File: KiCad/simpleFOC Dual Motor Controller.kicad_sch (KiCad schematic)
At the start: 17 parts, among them J101 Conn_01x04, J102 Conn_ARM_JTAG_SWD_10, SW101 TS-1088-AR02016, U101 STM32F103C8Tx, U102 XT60H-M

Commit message: updated configuration for new mosfets
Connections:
- net GAIN1: now reaches U101.2 (PC13)
- net GAIN2: now reaches U101.4 (PC15)
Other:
- sheet Motor Driver 1 ports: added Gain, ~{FAULT}; removed FAULT
- sheet Motor Driver 2 ports: added Gain, ~{FAULT}; removed FAULT
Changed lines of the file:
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@@
 	(wire
 		(pts
+			(xy 116.84 87.63) (xy 107.95 87.63)
+		)
+		(stroke
+			(width 0)
+			(type default)
+		)
+	)
+	(wire
+		(pts
 			(xy 135.89 149.86) (xy 134.62 149.86)
 		)
@@
 	(wire
 		(pts
+			(xy 116.84 92.71) (xy 107.95 92.71)
+		)
+		(stroke
+			(width 0)
+			(type default)
+		)
+	)
+	(wire
+		(pts
 			(xy 69.85 123.19) (xy 78.74 123.19)
 		)
@@
 	(wire
 		(pts
+			(xy 255.27 105.41) (xy 264.16 105.41)
+		)
+		(stroke
+			(width 0)
+			(type default)
+		)
+	)
+	(wire
+		(pts
 			(xy 50.8 63.5) (xy 58.42 63.5)
 		)
@@
 	(wire
 		(pts
+			(xy 255.27 58.42) (xy 264.16 58.42)
+		)
+		(stroke
+			(width 0)
+			(type default)
+		)
+	)
+	(wire
+		(pts
 			(xy 116.84 118.11) (xy 107.95 118.11)
 		)
@@
 		)
 	)
+	(label "GAIN1"
+		(at 107.95 87.63 0)
+		(effects
+			(font
+				(size 1.27 1.27)
+			)
+			(justify left bottom)
+		)
+	)
 	(label "sns_cs1"
 		(at 161.29 97.79 180)
@@
 		)
 	)
+	(label "GAIN2"
+		(at 107.95 92.71 0)
+		(effects
+			(font
+				(size 1.27 1.27)
+			)
+			(justify left bottom)
+		)
+	)
 	(label "FAULT1"
 		(at 107.95 128.27 0)
@@
 		)
 	)
+	(label "GAIN1"
+		(at 264.16 58.42 180)
+		(effects
+			(font
+				(size 1.27 1.27)
+			)
+			(justify right bottom)
+		)
+	)
 	(label "ctrl_scl"
 		(at 39.37 71.12 180)
@@
 		)
 	)
+	(label "GAIN2"
+		(at 264.16 105.41 180)
+		(effects
+			(font
+				(size 1.27 1.27)
+			)
+			(justify right bottom)
+		)
+	)
 	(label "CHCn2"
 		(at 205.74 127 0)
@@
 			)
 		)
-		(pin "FAULT" output
-			(at 214.63 60.96 180)
-			(effects
-				(font
-					(size 1.27 1.27)
-				)
-				(justify left)
-			)
-		)
 		(pin "INHA" input
 			(at 214.63 66.04 180)
@@
 			)
 		)
+		(pin "Gain" input
+			(at 255.27 58.42 0)
+			(effects
+				(font
+					(size 1.27 1.27)
+				)
+				(justify right)
+			)
+		)
+		(pin "~{FAULT}" output
+			(at 214.63 60.96 180)
+			(effects
+				(font
+					(size 1.27 1.27)
+				)
+				(justify left)
+			)
+		)
 		(instances
 			(project "simpleFOC Dual Motor Controller"
@@
 			)
 		)
-		(pin "FAULT" output
-			(at 214.63 107.95 180)
-			(effects
-				(font
-					(size 1.27 1.27)
-				)
-				(justify left)
-			)
-		)
 		(pin "INHA" input
 			(at 214.63 113.03 180)
@@
 			(effects
 				(font
+					(size 1.27 1.27)
+				)
+				(justify left)
+			)
+		)
+		(pin "Gain" input
+			(at 255.27 105.41 0)
+			(effects
+				(font
+					(size 1.27 1.27)
+				)
+				(justify right)
+			)
+		)
+		(pin "~{FAULT}" output
+			(at 214.63 107.95 180)
+			(effects
+				(font

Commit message: started laying out
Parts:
- removed C106, C107: 100n, symbol Device:C_Small
- removed D103: DSK26_C7502712, easyeda2kicad:SOD-123FL_L2.7-W1.8-LS3.8-RD, symbol easyeda2kicad:DSK26_C7502712
- removed H101, H102: MountingHole, MountingHole:MountingHole_4.3mm_M4, symbol Mechanical:MountingHole
- removed J102: Conn_ARM_JTAG_SWD_10, symbol Connector:Conn_ARM_JTAG_SWD_10
- removed U101: STM32F103C8Tx, Package_QFP:LQFP-48_7x7mm_P0.5mm, symbol MCU_ST_STM32F1:STM32F103C8Tx
- added C111: C_Small, Capacitor_SMD:C_01005_0402Metric, symbol Device:C_Small
- added D102, D107: B16WS_C7420327, easyeda2kicad:SOD-323_L1.7-W1.3-LS2.5-FD, symbol easyeda2kicad:B16WS_C7420327
- added D105, D106: H5VL06B, easyeda2kicad:X3-DFN0603-2_L0.6-W0.3-BI, symbol easyeda2kicad:H5VL06B
- added J102: USB_C_Receptacle_USB2.0_14P, Connector_USB:USB_C_Receptacle_HCTL_HC-TYPE-C-16P-01A, symbol Connector:USB_C_Receptacle_USB2.0_14P
- added R107, R108: 5.1k, PCM_SparkFun-Resistor:R_0402_1005Metric, symbol Device:R_Small
- added R109: 10k, PCM_SparkFun-Resistor:R_0402_1005Metric, symbol Device:R_Small
- added U101: XC6206P332MR, easyeda2kicad:SOT-23-3_L2.9-W1.6-P1.90-LS2.8-BR, symbol easyeda2kicad:XC6206P332MR
- added U103: ESP32-S3-WROOM-1, RF_Module:ESP32-S3-WROOM-1, symbol RF_Module:ESP32-S3-WROOM-1
- C103: footprint (none) -> Capacitor_SMD:C_01005_0402Metric
- C104: value 100n -> 22u; footprint (none) -> Capacitor_SMD:C_1206_3216Metric
- C105: value 100n -> 1u; footprint (none) -> Capacitor_SMD:C_01005_0402Metric
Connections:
- net +3.3V: now also R109.1, U101.2 (Vout), U103.2 (3V3); no longer C102.1, C105.1
- net CAL1: now also U103.31 (IO38)
- net CAL2: now also U103.8 (IO15)
- net CHA1: now also U103.35 (IO42)
- net CHA2: now also U103.5 (IO5)
- net CHB1: now also U103.34 (IO41)
- net CHB2: now also U103.6 (IO6)
- net CHC1: now also U103.33 (IO40)
- net CHC2: now also U103.7 (IO7)
- net EN1: now also U103.32 (IO39)
- net EN2: now also U103.12 (IO8)
- net FAULT1: now also U103.28 (IO35)
- net FAULT2: now also U103.18 (IO10)
- net GAIN1: now also U103.29 (IO36)
- net GAIN2: now also U103.19 (IO11)
- net GND: now also C111.2, D105.1 (C), D106.1 (C), J102.A1 (GND), J102.A12 (GND), J102.B1 (GND), J102.B12 (GND), J102.SH (SHIELD), R107.2, R108.2, U101.1 (GND), U103.1 (GND), U103.40 (GND), U103.41 (GND)
- net ctrl_scl: now also U103.20 (IO12)
- net ctrl_sda: now also U103.21 (IO13)
- net snsA1: now also U103.39 (IO1)
- net snsA2: now also U103.9 (IO16)
- net snsB1: now also U103.38 (IO2)
- net snsB2: now also U103.10 (IO17)
- net snsC1: now also U103.4 (IO4)
- net snsC2: now also U103.11 (IO18)
- net sns_cs1: now also U103.17 (IO9)
- net sns_cs2: now also U103.23 (IO21)
- net sns_miso: now also U103.24 (IO47)
- net sns_mosi: now also U103.25 (IO48)
- net sns_sck: now also U103.22 (IO14)
- net ~{rst}: now also C111.1, R109.2, U103.3 (EN)
- net at D104.1 (K), J101.4 (Pin_4): now also D107.1 (A)
- new net: J102.B5 (CC2), R108.1
- new net: D102.1 (A), J102.A4 (VBUS), J102.A9 (VBUS), J102.B4 (VBUS), J102.B9 (VBUS)
- new net: J102.A5 (CC1), R107.1
- new net +5V: C102.1, C105.1, D102.2 (K), D107.2 (K), U101.3 (Vin)
- new net D+: D106.2 (A), J102.A6 (D+), J102.B6 (D+), U103.14 (USB_D+)
- new net D-: D105.2 (A), J102.A7 (D-), J102.B7 (D-), U103.13 (USB_D-)
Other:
- sheet Motor Driver 1 ports: added ~{HI-Z}; removed INLA, INLB, INLC
- sheet Motor Driver 2 ports: added ~{HI-Z}; removed INLA, INLB, INLC
- moved on the sheet: C103, SW101

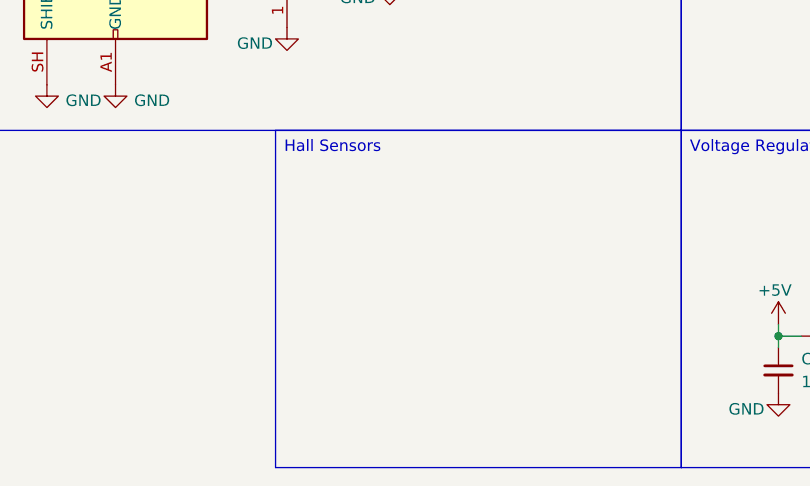
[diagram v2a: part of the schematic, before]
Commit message: added hall connectors
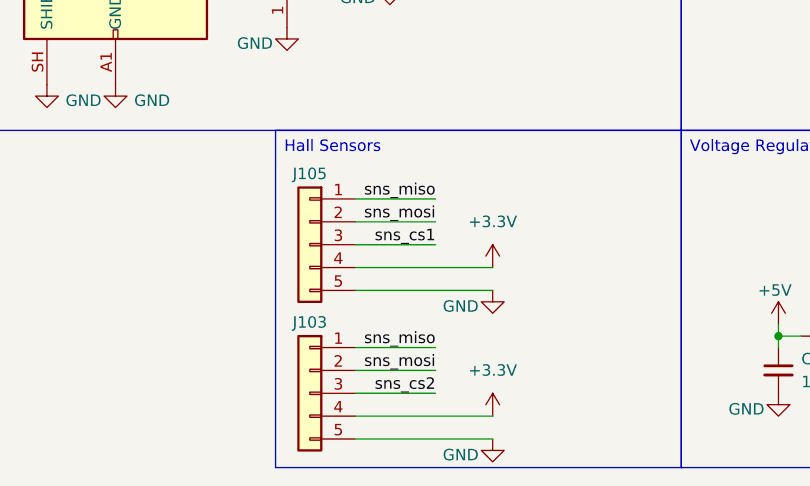
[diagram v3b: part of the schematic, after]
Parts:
- added J103, J105: Conn_01x05_2.0mm, Connector_JST:JST_PH_B5B-PH-K_1x05_P2.00mm_Vertical, symbol PCM_SparkFun-Connector:Conn_01x05_P2.0mm_Socket_Vertical_PTH
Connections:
- net +3.3V: now also J103.4 (Pin_4), J105.4 (Pin_4)
- net GND: now also J103.5 (Pin_5), J105.5 (Pin_5)
- net sns_cs1: now also J105.3 (Pin_3)
- net sns_cs2: now also J103.3 (Pin_3)
- net sns_miso: now also J103.1 (Pin_1), J105.1 (Pin_1)
- net sns_mosi: now also J103.2 (Pin_2), J105.2 (Pin_2)

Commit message: started routing
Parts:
- C105: footprint Capacitor_SMD:C_01005_0402Metric -> Capacitor_SMD:C_0402_1005Metric
- J101: footprint PCM_SparkFun-Connector:JST_1x04_P2.0mm_Vertical_PTH -> Connector_JST:JST_PH_B4B-PH-K_1x04_P2.00mm_Vertical
- R108: footprint PCM_SparkFun-Resistor:R_0402_1005Metric -> Resistor_SMD:R_0402_1005Metric
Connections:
- net CAL1: now also U103.12 (IO8); no longer U103.31 (IO38)
- net CAL2: now also U103.31 (IO38); no longer U103.8 (IO15)
- net CHA2: now also U103.30 (IO37); no longer U103.5 (IO5)
- net CHB1: now also U103.18 (IO10); no longer U103.34 (IO41)
- net CHB2: now also U103.29 (IO36); no longer U103.6 (IO6)
- net CHC1: now also U103.6 (IO6); no longer U103.33 (IO40)
- net CHC2: now also U103.28 (IO35); no longer U103.7 (IO7)
- net EN1: now also U103.8 (IO15); no longer U103.32 (IO39)
- net EN2: now also U103.32 (IO39); no longer U103.12 (IO8)
- net FAULT1: now also U103.7 (IO7); no longer U103.28 (IO35)
- net FAULT2: now also U103.34 (IO41); no longer U103.18 (IO10)
- net GAIN1: now also U103.19 (IO11); no longer U103.29 (IO36)
- net GAIN2: now also U103.33 (IO40); no longer U103.19 (IO11)
- net snsA1: now also U103.11 (IO18); no longer U103.39 (IO1)
- net snsA2: now also U103.39 (IO1); no longer U103.9 (IO16)
- net snsB1: now also U103.10 (IO17); no longer U103.38 (IO2)
- net snsB2: now also U103.38 (IO2); no longer U103.10 (IO17)
- net snsC2: now also U103.22 (IO14); no longer U103.11 (IO18)
- net sns_sck: now also U103.15 (IO3); no longer U103.22 (IO14)
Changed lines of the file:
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@@
 	(wire
 		(pts
-			(xy 130.81 175.26) (xy 132.08 175.26)
+			(xy 130.81 175.26) (xy 133.35 175.26)
 		)
 		(stroke
@@
 	(wire
 		(pts
-			(xy 109.22 120.65) (xy 118.11 120.65)
-		)
-		(stroke
-			(width 0)
-			(type default)
-		)
-	)
-	(wire
-		(pts
 			(xy 266.7 102.87) (xy 266.7 55.88)
 		)
@@
 	(wire
 		(pts
+			(xy 109.22 87.63) (xy 118.11 87.63)
+		)
+		(stroke
+			(width 0)
+			(type default)
+		)
+	)
+	(wire
+		(pts
 			(xy 31.75 66.04) (xy 44.45 66.04)
 		)
@@
 	(wire
 		(pts
-			(xy 118.11 92.71) (xy 109.22 92.71)
-		)
-		(stroke
-			(width 0)
-			(type default)
-		)
-	)
-	(wire
-		(pts
 			(xy 86.36 49.53) (xy 86.36 48.26)
 		)
@@
 	(wire
 		(pts
+			(xy 148.59 97.79) (xy 157.48 97.79)
+		)
+		(stroke
+			(width 0)
+			(type default)
+		)
+	)
+	(wire
+		(pts
 			(xy 54.61 91.44) (xy 63.5 91.44)
 		)
@@
 		)
 	)
+	(label "CHA2"
+		(at 157.48 97.79 180)
+		(effects
+			(font
+				(size 1.27 1.27)
+			)
+			(justify right bottom)
+		)
+	)
 	(label "CAL1"
 		(at 205.74 55.88 0)
@@
 	)
 	(label "CHB1"
-		(at 157.48 107.95 180)
+		(at 109.22 105.41 0)
 		(effects
 			(font
 				(size 1.27 1.27)
 			)
-			(justify right bottom)
+			(justify left bottom)
 		)
 	)
@@
 	)
 	(label "CHB2"
-		(at 109.22 95.25 0)
+		(at 157.48 95.25 180)
 		(effects
 			(font
 				(size 1.27 1.27)
 			)
-			(justify left bottom)
+			(justify right bottom)
 		)
 	)
@@
 		)
 	)
+	(label "snsA2"
+		(at 109.22 82.55 0)
+		(effects
+			(font
+				(size 1.27 1.27)
+			)
+			(justify left bottom)
+		)
+	)
 	(label "ctrl_scl"
 		(at 109.22 110.49 0)
@@
 	)
 	(label "snsB2"
-		(at 157.48 80.01 180)
+		(at 109.22 85.09 0)
 		(effects
 			(font
 				(size 1.27 1.27)
 			)
-			(justify right bottom)
+			(justify left bottom)
 		)
 	)
@@
 	)
 	(label "snsB1"
-		(at 109.22 85.09 0)
+		(at 157.48 80.01 180)
 		(effects
 			(font
 				(size 1.27 1.27)
 			)
-			(justify left bottom)
+			(justify right bottom)
 		)
 	)
@@
 	)
 	(label "CHA2"
-		(at 109.22 92.71 0)
-		(effects
-			(font
-				(size 1.27 1.27)
-			)
-			(justify left bottom)
-		)
-	)
-	(label "CHA2"
 		(at 207.01 118.11 0)
 		(effects
@@
 	)
 	(label "CHC2"
-		(at 109.22 97.79 0)
+		(at 157.48 92.71 180)
 		(effects
 			(font
 				(size 1.27 1.27)
 			)
-			(justify left bottom)
+			(justify right bottom)
 		)
 	)
 	(label "snsC2"
-		(at 157.48 82.55 180)
+		(at 109.22 115.57 0)
 		(effects
 			(font
 				(size 1.27 1.27)
 			)
-			(justify right bottom)
+			(justify left bottom)
 		)
 	)
 	(label "sns_sck"
-		(at 109.22 115.57 0)
+		(at 109.22 87.63 0)
 		(effects
 			(font
@@
 	)
 	(label "EN2"
-		(at 109.22 100.33 0)
+		(at 157.48 102.87 180)
 		(effects
 			(font
 				(size 1.27 1.27)
 			)
-			(justify left bottom)
+			(justify right bottom)
 		)
 	)
@@
 	)
 	(label "FAULT1"
-		(at 157.48 92.71 180)
+		(at 109.22 97.79 0)
 		(effects
 			(font
 				(size 1.27 1.27)
 			)
-			(justify right bottom)
+			(justify left bottom)
 		)
 	)
@@
 	)
 	(label "EN1"
-		(at 157.48 102.87 180)
+		(at 109.22 118.11 0)
 		(effects
 			(font
 				(size 1.27 1.27)
 			)
-			(justify right bottom)
+			(justify left bottom)
 		)
 	)
 	(label "CHC1"
-		(at 157.48 105.41 180)
+		(at 109.22 95.25 0)
 		(effects
 			(font
 				(size 1.27 1.27)
 			)
-			(justify right bottom)
+			(justify left bottom)
 		)
 	)
@@
 	)
 	(label "GAIN2"
-		(at 109.22 107.95 0)
+		(at 157.48 105.41 180)
 		(effects
 			(font
 				(size 1.27 1.27)
 			)
-			(justify left bottom)
+			(justify right bottom)
 		)
 	)
@@
 	)
 	(label "CAL2"
-		(at 109.22 118.11 0)
+		(at 157.48 100.33 180)
 		(effects
 			(font
 				(size 1.27 1.27)
 			)
-			(justify left bottom)
+			(justify right bottom)
 		)
 	)
 	(label "snsA1"
-		(at 109.22 82.55 0)
+		(at 157.48 82.55 180)
 		(effects
 			(font
 				(size 1.27 1.27)
 			)
-			(justify left bottom)
+			(justify right bottom)
 		)
 	)
@@
 	)
 	(label "FAULT2"
-		(at 109.22 105.41 0)
+		(at 157.48 107.95 180)
 		(effects
 			(font
 				(size 1.27 1.27)
 			)
-			(justify left bottom)
+			(justify right bottom)
 		)
 	)
 	(label "CAL1"
-		(at 157.48 100.33 180)
+		(at 109.22 100.33 0)
 		(effects
 			(font
 				(size 1.27 1.27)
 			)
-			(justify right bottom)
+			(justify left bottom)
 		)
 	)
@@
 	)
 	(label "GAIN1"
-		(at 157.48 95.25 180)
+		(at 109.22 107.95 0)
 		(effects
 			(font
 				(size 1.27 1.27)
 			)
-			(justify right bottom)
+			(justify left bottom)
 		)
 	)
@@
 		)
 	)
-	(label "snsA2"
-		(at 109.22 120.65 0)
-		(effects
-			(font
-				(size 1.27 1.27)
-			)
-			(justify left bottom)
-		)
-	)
 	(label "ctrl_sda"
 		(at 109.22 113.03 0)
@@
 			)
 		)
-		(property "Footprint" "Capacitor_SMD:C_01005_0402Metric"
+		(property "Footprint" "Capacitor_SMD:C_0402_1005Metric"
 			(at 107.95 184.15 0)
 			(hide yes)
@@
 			)
 		)
-		(property "Footprint" "PCM_SparkFun-Resistor:R_0402_1005Metric"
+		(property "Footprint" "Resistor_SMD:R_0402_1005Metric"
 			(at 76.2 124.46 0)
 			(hide yes)
@@
 			)
 		)
-		(property "Footprint" "PCM_SparkFun-Connector:JST_1x04_P2.0mm_Vertical_PTH"
+		(property "Footprint" "Connector_JST:JST_PH_B4B-PH-K_1x04_P2.00mm_Vertical"
 			(at 26.67 58.42 0)
 			(hide yes)
@@
 	(symbol
 		(lib_id "power:+3.3V")
-		(at 132.08 175.26 0)
+		(at 133.35 175.26 0)
 		(unit 1)
 		(body_style 1)
@@
 		(fields_autoplaced yes)
 		(property "Reference" "#PWR0128"
-			(at 132.08 179.07 0)
+			(at 133.35 179.07 0)
 			(hide yes)
 			(show_name no)
@@
 		)
 		(property "Value" "+3.3V"
-			(at 132.08 170.18 0)
+			(at 133.35 170.18 0)
 			(show_name no)
 			(do_not_autoplace no)
@@
 		)
 		(property "Footprint" ""
-			(at 132.08 175.26 0)
+			(at 133.35 175.26 0)
 			(hide yes)
 			(show_name no)
@@
 		)
 		(property "Datasheet" ""
-			(at 132.08 175.26 0)
+			(at 133.35 175.26 0)
 			(hide yes)
 			(show_name no)
@@
 		)
 		(property "Description" "Power symbol creates a global label with name \"+3.3V\""
-			(at 132.08 175.26 0)
+			(at 133.35 175.26 0)
 			(hide yes)
 			(show_name no)

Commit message: mostly finished routing
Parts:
- removed D104: SMF5.0A_C19077497, easyeda2kicad:SOD-123FL_L2.7-W1.8-LS3.8-RD, symbol easyeda2kicad:SMF5.0A_C19077497
- removed J103, J105: Conn_01x05_2.0mm, Connector_JST:JST_PH_B5B-PH-K_1x05_P2.00mm_Vertical, symbol PCM_SparkFun-Connector:Conn_01x05_P2.0mm_Socket_Vertical_PTH
- added J103, J104: Conn_01x06, Connector_JST:JST_PH_B6B-PH-K_1x06_P2.00mm_Vertical, symbol Connector_Generic:Conn_01x06
- added R110, R111: 100k, Resistor_SMD:R_0402_1005Metric, symbol Device:R_Small
- added U104: H5VND5UB, easyeda2kicad:SOD-523F_L1.7-W0.9-LS1.7-RD, symbol easyeda2kicad:H5VND5UB
- C101: value 470u -> 220u; footprint (none) -> easyeda2kicad:CAP-TH_BD8.0-P3.50-D0.6-FD
- C103: footprint Capacitor_SMD:C_01005_0402Metric -> Capacitor_SMD:C_0402_1005Metric
- C104: footprint Capacitor_SMD:C_1206_3216Metric -> Capacitor_SMD:C_0603_1608Metric
- C111: value C_Small -> 1u; footprint Capacitor_SMD:C_01005_0402Metric -> Capacitor_SMD:C_0402_1005Metric
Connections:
- net +3.3V: now also J103.5 (Pin_5), J104.5 (Pin_5), R110.2, R111.2
- net +5V: now also U104.1 (K)
- net CAL1: now also U103.7 (IO7); no longer U103.12 (IO8)
- net CHA1: now also U103.12 (IO8); no longer U103.35 (IO42)
- net CHB1: now also U103.11 (IO18); no longer U103.18 (IO10)
- net CHC1: now also U103.10 (IO17); no longer U103.6 (IO6)
- net EN1: now also U103.6 (IO6); no longer U103.8 (IO15)
- net FAULT1: now also U103.20 (IO12); no longer U103.7 (IO7)
- net GND: now also J103.6 (Pin_6), J104.6 (Pin_6), U104.2 (A)
- net ctrl_scl: now also U103.9 (IO16); no longer U103.20 (IO12)
- net ctrl_sda: now also U103.8 (IO15); no longer U103.21 (IO13)
- net snsA1: now also U103.15 (IO3); no longer U103.11 (IO18)
- net snsA2: now also U103.38 (IO2); no longer U103.39 (IO1)
- net snsB1: now also U103.17 (IO9); no longer U103.10 (IO17)
- net snsB2: now also U103.39 (IO1); no longer U103.38 (IO2)
- net snsC1: now also U103.18 (IO10); no longer U103.4 (IO4)
- net sns_cs1: now also U103.21 (IO13), J104.4 (Pin_4), R110.1; no longer U103.17 (IO9)
- net sns_cs2: now also U103.35 (IO42), J103.4 (Pin_4), R111.1; no longer U103.23 (IO21)
- net sns_miso: now also J103.2 (Pin_2), J104.2 (Pin_2)
- net sns_mosi: now also J103.1 (Pin_1), J104.1 (Pin_1)
- net sns_sck: now also U103.23 (IO21), J103.3 (Pin_3), J104.3 (Pin_3); no longer U103.15 (IO3)
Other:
- moved on the sheet: C105, U101
